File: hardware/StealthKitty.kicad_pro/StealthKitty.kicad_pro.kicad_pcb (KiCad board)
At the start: 4 copper layers, 54 x 57 mm, 89 parts, among them J1 Conn_01x08, J2 Conn_01x06, J3 Conn_01x06, J5 Conn_ST_STDC14, J7 Conn_01x06, J9 Conn_01x06, SW1 SW_Push, SW2 SW_Push, SW5 Switch, U2 ZXBM5210-S, U3 ZXBM5210-S, U4 MP1475DJ-LF-P, U5 ADXL343, U6 STM32G431CBU6, Y1 Crystal_GND24_Small

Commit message: Confirmation placement equipe
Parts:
- removed U4: MP1475DJ-LF-P, Library:SOT65P280X100-8N
- added IC501: MP1475DJ-LF-P, Library:SOT65P280X100-8N, F.Cu at (125.0, 69.0)
- moved D201 0.40 mm to (115.5, 69.6)
- moved R201 0.40 mm to (111.5, 69.6)
- moved TP309 0.25 mm to (135.0, 75.2)
- moved TP310 0.25 mm to (131.8, 75.2)
- moved C505 0.20 mm to (125.5, 64.3)
- moved R503 0.20 mm to (125.0, 65.8)
- renumbered Alim_charger2 to Alim_charger501, BT2 to BT501, C3 to C201, C4 to C202, C5 to C203, C6 to C204, C7 to C205, C8 to C206, C9 to C207, C10 to C208, C11 to C401, C19 to C402, C20 to C403, C12 to C404, C21 to C405, C1 to C406, C13 to C407, C22 to C408, C14 to C409, C23 to C410, C15 to C411, C35 to C501, C27 to C502, C26 to C503, C28 to C504, C36 to C505, C29 to C506, C39 to C507, C37 to C508, C38 to C509, Cio1 to Cio301, Cs1 to Cs301, D1 to D201, D2 to D202, D3 to D203, D4 to D204, D7 to D401, D5 to D402, D6 to D501, J2 to J201, J3 to J202, J7 to J301, J9 to J302, J1 to J303, J5 to J401, L3 to L501, PS2 to PS501, R5 to R201, R6 to R202, R7 to R203, R8 to R204, R9 to R401, R10 to R402, R17 to R403, R3 to R404, R22 to R501, R1 to R502, R23 to R503, R24 to R504, R25 to R505, R26 to R506, R21 to R507, SW1 to SW401, SW2 to SW402, SW5 to SW501, TP204 to TP203, TP203 to TP204, TP4 to TP301, TP3 to TP302, TP1 to TP303, TP2 to TP304, TP5 to TP305, TP6 to TP306, TP7 to TP307, TP9 to TP308, TP11 to TP309, TP10 to TP310, U2 to U201, U3 to U202, U5 to U301, U6 to U401, Y1 to Y401

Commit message: après première revue fiack placement
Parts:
- removed U201, U202: ZXBM5210-S, Package_SO:SOIC-8_3.9x4.9mm_P1.27mm
- added U1: ZXBM5210-SP, Package_SO:Diodes_SO-8EP, F.Cu at (113.5, 75.5)
- added U2: ZXBM5210-SP, Package_SO:Diodes_SO-8EP, F.Cu at (113.5, 91.0)
- moved Cio301 6.92 mm to (120.7, 72.1)
- moved Cs301 5.79 mm to (120.5, 75.0), turned to -90 degrees
- moved TP308 4.60 mm to (128.2, 74.6)
- moved C410 3.88 mm to (128.1, 71.6)
- moved C408 1.71 mm to (126.3, 77.2), turned to 180 degrees
- moved U301 0.32 mm to (123.1, 73.7), turned to 0 degrees
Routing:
- net +5V: track 0.00 -> 77.9 mm
- net MOSI: track 0.00 -> 9.34 mm
- net GND: vias 0 -> 17
- added copper zone on B.Cu, net GND
- added copper zone on F.Cu, net GND
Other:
- board text added: "TOF1"

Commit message: Dernier Modif 08/10/2024
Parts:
- removed D201: Blue, LED_SMD:LED_0603_1608Metric_Pad1.05x0.95mm_HandSolder
- removed D202: YELLOW, LED_SMD:LED_0603_1608Metric_Pad1.05x0.95mm_HandSolder
- removed D203: Green, LED_SMD:LED_0603_1608Metric_Pad1.05x0.95mm_HandSolder
- removed D204: RED, LED_SMD:LED_0603_1608Metric_Pad1.05x0.95mm_HandSolder
- removed R201, R202: 100R, Resistor_SMD:R_0603_1608Metric_Pad0.98x0.95mm_HandSolder
- removed R203, R204: 1k, Resistor_SMD:R_0603_1608Metric_Pad0.98x0.95mm_HandSolder
- removed TP306: TestPoint, TestPoint:TestPoint_Pad_D1.5mm
- added TP301: TestPoint, TestPoint:TestPoint_Pad_D1.5mm, F.Cu at (186.5, 93.5)
- added TP302: TestPoint, TestPoint:TestPoint_Pad_D1.5mm, F.Cu at (186.5, 97.0)
- BT501: footprint Connector_JST:JST_XH_S2B-XH-A-1_1x02_P2.50mm_Horizontal -> Connector_JST:JST_XH_S2B-XH-A_1x02_P2.50mm_Horizontal
- C201, C202, C203, C207, C208, C402, C407, C410, C504, C506, Cs301: footprint Capacitor_SMD:C_0603_1608Metric_Pad1.08x0.95mm_HandSolder -> Capacitor_SMD:C_0402_1005Metric
- C204, C205, C206, C401, C403, C404, C405, C406, C408, C409, C411, C502, C505, C508, Cio301: footprint Capacitor_SMD:C_0402_1005Metric_Pad0.74x0.62mm_HandSolder -> Capacitor_SMD:C_0402_1005Metric
- C501: value 0.1uF -> 22uF; footprint Capacitor_SMD:C_0402_1005Metric_Pad0.74x0.62mm_HandSolder -> Capacitor_SMD:C_0402_1005Metric
- C503: value 22uF -> 0.1uF; footprint Capacitor_SMD:C_0805_2012Metric_Pad1.18x1.45mm_HandSolder -> Capacitor_SMD:C_0402_1005Metric
- C507, C509: footprint Capacitor_SMD:C_0805_2012Metric_Pad1.18x1.45mm_HandSolder -> Capacitor_SMD:C_0402_1005Metric
- J301, J302: footprint Connector_JST:JST_XH_B6B-XH-A_1x06_P2.50mm_Vertical -> Connector_JST:JST_XH_S6B-XH-A_1x06_P2.50mm_Horizontal
- R401, R402, R403, R404, R501, R502, R503, R504, R505, R506, R507: footprint Resistor_SMD:R_0603_1608Metric_Pad0.98x0.95mm_HandSolder -> Resistor_SMD:R_0402_1005Metric
- SW401, SW402: footprint Button_Switch_SMD:SW_SPST_B3U-1000P -> Button_Switch_SMD:SW_Push_1P1T_NO_6x6mm_H9.5mm
- SW501: footprint Connector_JST:JST_XH_S3B-XH-A_1x03_P2.50mm_Horizontal -> Connector_JST:JST_XH_S3B-XH-A-1_1x03_P2.50mm_Horizontal
- moved TP305 76.6 mm to (187.0, 103.0)
- moved TP301 66.7 mm to (199.3, 121.0)
- moved TP302 66.7 mm to (202.3, 121.0)
- moved TP303 66.7 mm to (201.5, 118.0)
- moved TP304 66.7 mm to (204.1, 118.0)
- moved TP307 61.7 mm to (195.5, 84.3)
- moved TP309 61.7 mm to (195.5, 87.5)
- moved TP310 61.7 mm to (192.2, 87.5)
- moved J202 45.5 mm to (132.9, 99.0)
- moved C501 44.7 mm to (157.7, 90.3), turned to 0 degrees
- moved C503 42.8 mm to (157.7, 89.3), turned to 0 degrees
- moved C504 42.1 mm to (150.4, 80.8), turned to 180 degrees
- moved C509 40.5 mm to (162.3, 91.3), turned to 180 degrees
- moved PS501 40.1 mm to (150.1, 83.5), turned to -90 degrees
- moved R503 39.9 mm to (160.0, 85.0), turned to 90 degrees
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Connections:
- U401 pad 17: /brain Sheet/status_Purple -> unconnected-(U401-PB0-Pad17)
- U401 pad 18: unconnected-(U401-PB1-Pad18) -> INT2_adx
- U401 pad 19: /brain Sheet/Button_1 -> INT1_adx
- U401 pad 26: unconnected-(U401-PB13-Pad26) -> /brain Sheet/status_Orange
- U401 pad 27: /brain Sheet/status_Orange -> /brain Sheet/status_Purple
- U401 pad 28: unconnected-(U401-PB15-Pad28) -> /brain Sheet/Button_1
- U401 pad 8: INT1_adx -> unconnected-(U401-PA0-Pad8)
- U401 pad 9: INT2_adx -> unconnected-(U401-PA1-Pad9)
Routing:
- net /motorisation Sheet/Motor2-: track 0.00 -> 77.9 mm
- net +5V: track 77.9 -> 0.00 mm
- net SDA: track 0.00 -> 23.5 mm
- net SCL: track 0.00 -> 17.1 mm
- net MOSI: track 9.34 -> 0.00 mm
- net GND: vias 17 -> 25

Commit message: Modification Placement 09/10/24
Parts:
- removed the TP301 at (199.3, 121.0)
- removed the TP302 at (202.3, 121.0)
- removed TP303, TP304, TP305: TestPoint, TestPoint:TestPoint_Pad_D1.5mm
- BT501: footprint Connector_JST:JST_XH_S2B-XH-A_1x02_P2.50mm_Horizontal -> Connector_JST:JST_XH_S2B-XH-A-1_1x02_P2.50mm_Horizontal
- moved TP309 48.5 mm to (147.4, 93.4)
- moved TP310 45.0 mm to (147.4, 90.7)
- moved C404 44.8 mm to (155.8, 105.9), turned to 0 degrees
- moved C407 42.5 mm to (150.4, 95.5), turned to 0 degrees
- moved C402 41.7 mm to (154.6, 95.5), turned to 180 degrees
- moved C406 39.2 mm to (148.3, 95.5), turned to 180 degrees
- moved TP302 38.4 mm to (149.1, 88.1)
- moved C405 38.4 mm to (152.5, 95.5), turned to 0 degrees
- moved TP307 37.8 mm to (159.3, 95.2)
- moved C401 35.3 mm to (147.3, 102.5), turned to 90 degrees
- moved TP301 27.6 mm to (159.3, 98.2)
- moved R401 4.07 mm to (155.8, 117.2)
- moved C408 2.80 mm to (156.5, 92.2)
- moved R402 2.28 mm to (158.1, 117.2)
- moved C410 2.20 mm to (149.5, 92.3)
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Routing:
- net SDA: track 23.5 -> 0.00 mm
- net SCL: track 17.1 -> 0.00 mm
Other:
- board size 54 x 57 mm -> 54 x 58.9 mm

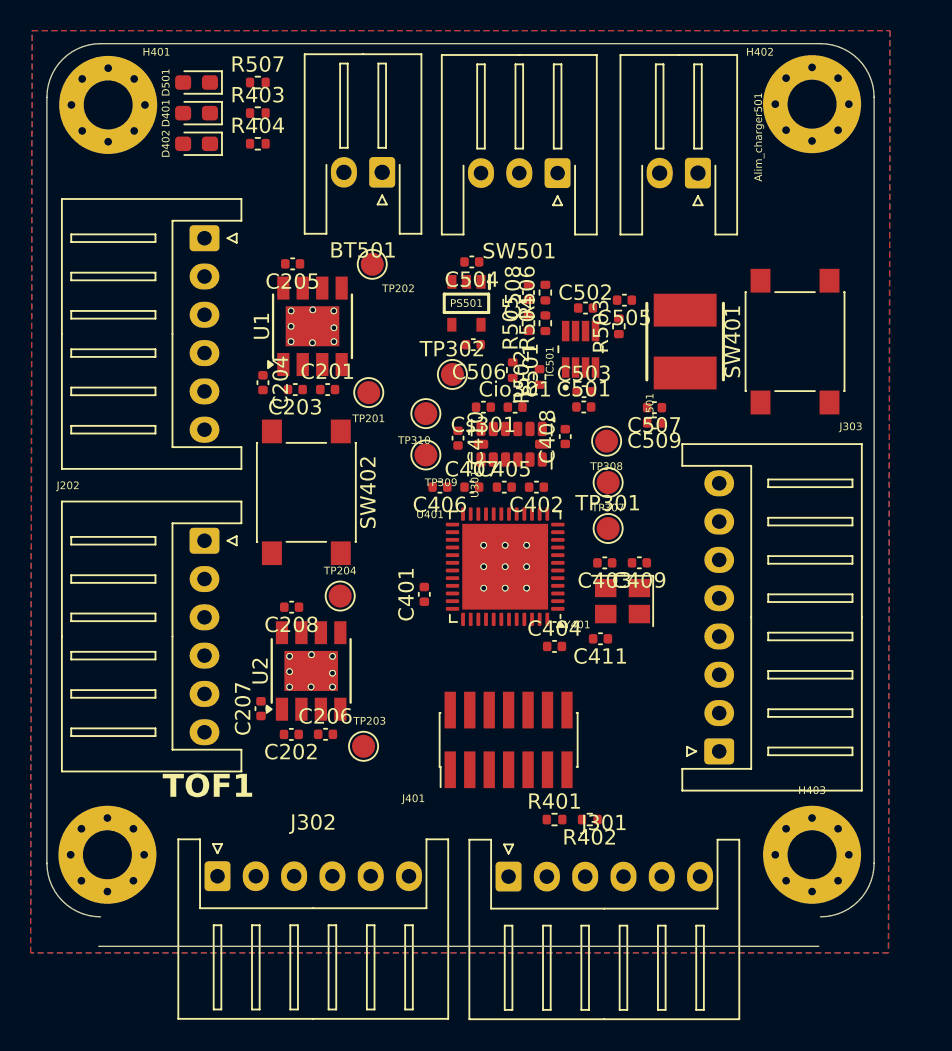
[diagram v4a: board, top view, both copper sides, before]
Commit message: Début routage
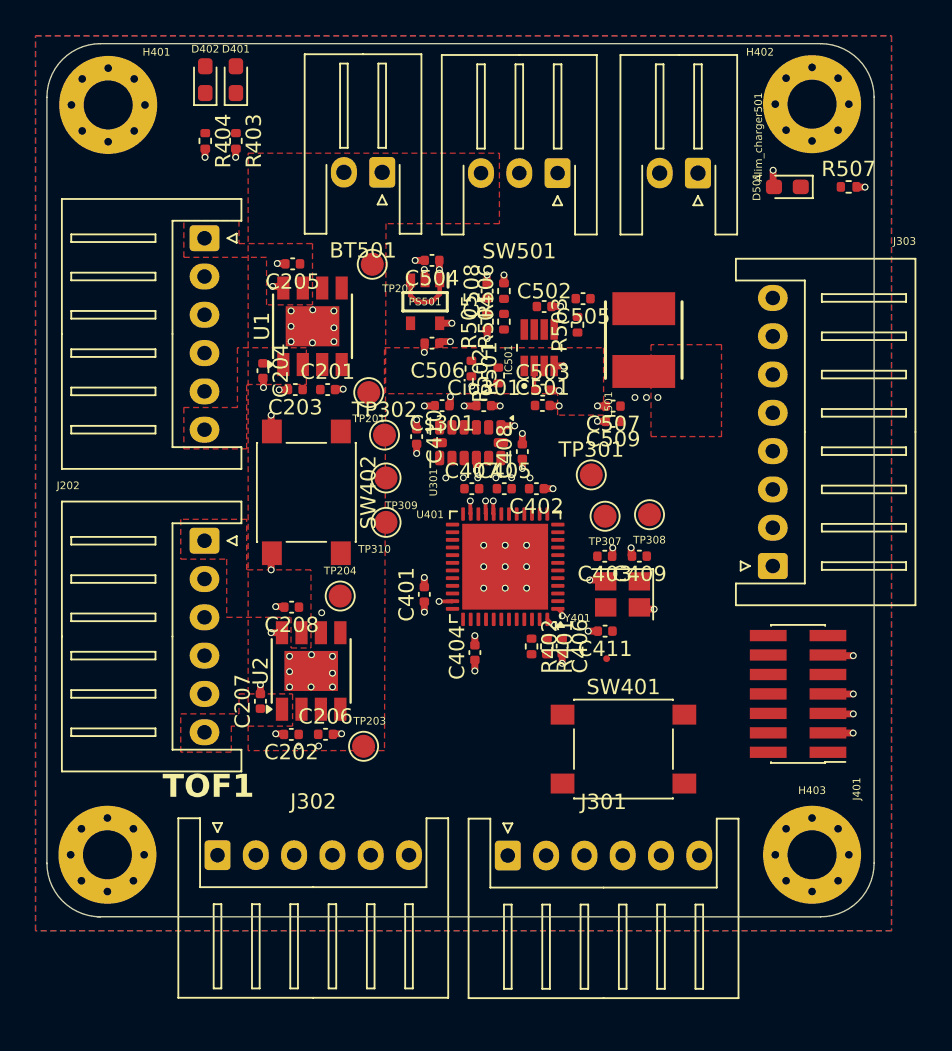
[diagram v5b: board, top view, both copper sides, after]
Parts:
- moved D501 39.2 mm to (171.0, 75.9)
- moved R507 39.2 mm to (175.0, 75.9)
- moved SW401 28.9 mm to (160.3, 112.6), turned to 0 degrees
- moved J401 19.1 mm to (171.7, 109.0), turned to 180 degrees
- moved C406 13.1 mm to (156.3, 105.9), turned to -90 degrees
- moved J303 12.6 mm to (170.1, 100.7)
- moved R402 11.9 mm to (154.3, 105.9), turned to -90 degrees
- moved R401 11.3 mm to (155.3, 105.9), turned to -90 degrees
- moved TP310 7.56 mm to (144.8, 97.8)
- moved TP302 5.94 mm to (144.7, 92.1)
- moved TP308 5.56 mm to (162.0, 97.3)
- moved C404 5.22 mm to (150.6, 106.3), turned to 90 degrees
- moved D402 4.22 mm to (133.0, 68.9), turned to 90 degrees
- moved TP301 3.67 mm to (158.2, 94.7)
- moved R404 3.44 mm to (133.0, 72.9), turned to -90 degrees
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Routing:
- net /motorisation Sheet/Motor2-: track 77.9 -> 0.00 mm
- net +5V: track 0.00 -> 70.9 mm, vias 0 -> 6
- net GND: track 0.00 -> 30.7 mm, vias 25 -> 70
- net +3.3V: track 0.00 -> 14.2 mm, vias 0 -> 21
- net +VBAT: track 0.00 -> 1.61 mm, vias 0 -> 4
- added copper zone on F.Cu, net +5V
- added copper zone on In2.Cu, net +5V
- added copper zone on F.Cu, net +VBAT
- added copper zone on In2.Cu, net +VBAT
- added copper zone on F.Cu, net /motorisation Sheet/Motor1+
- added copper zone on F.Cu, net /motorisation Sheet/Motor1-
- added copper zone on F.Cu, net /motorisation Sheet/Motor2+
- added copper zone on F.Cu, net /motorisation Sheet/Motor2-
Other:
- board size 54 x 58.9 mm -> 54 x 57 mm

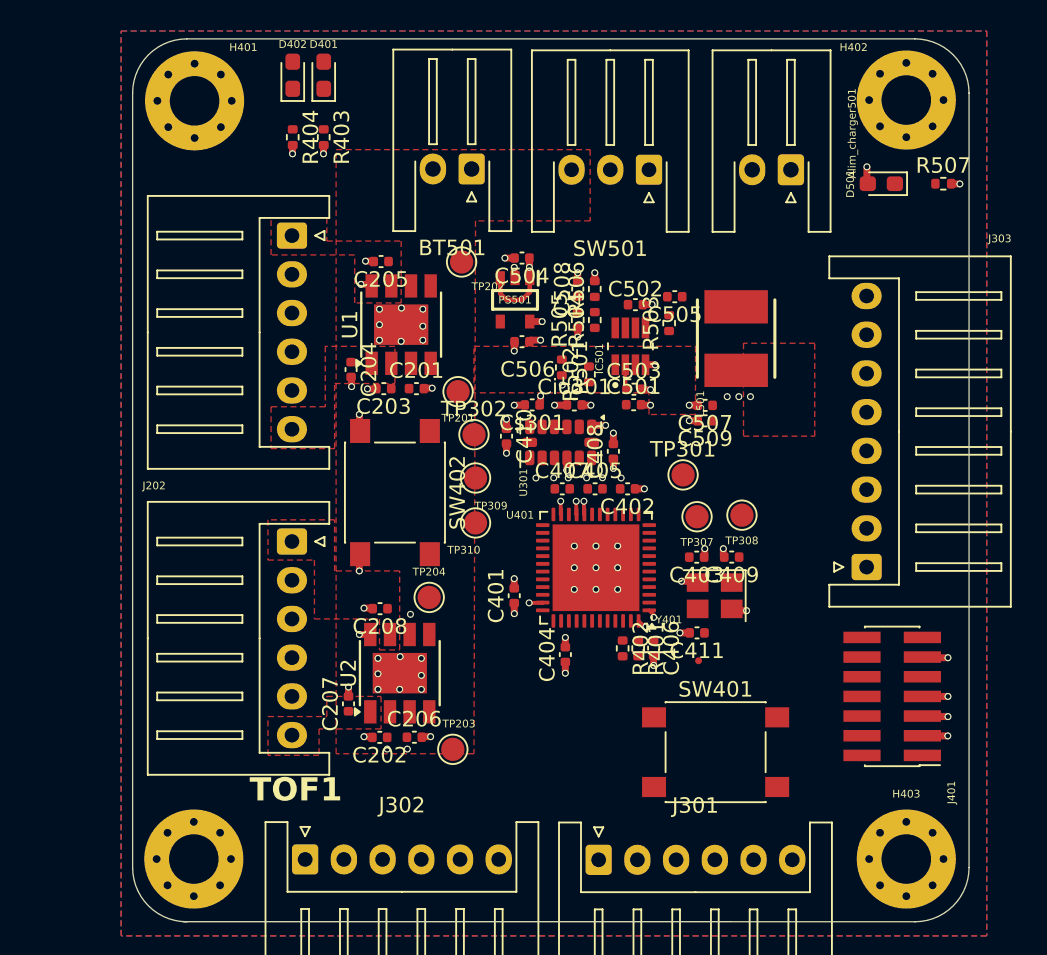
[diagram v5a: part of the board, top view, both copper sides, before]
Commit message: MAJ première version routage
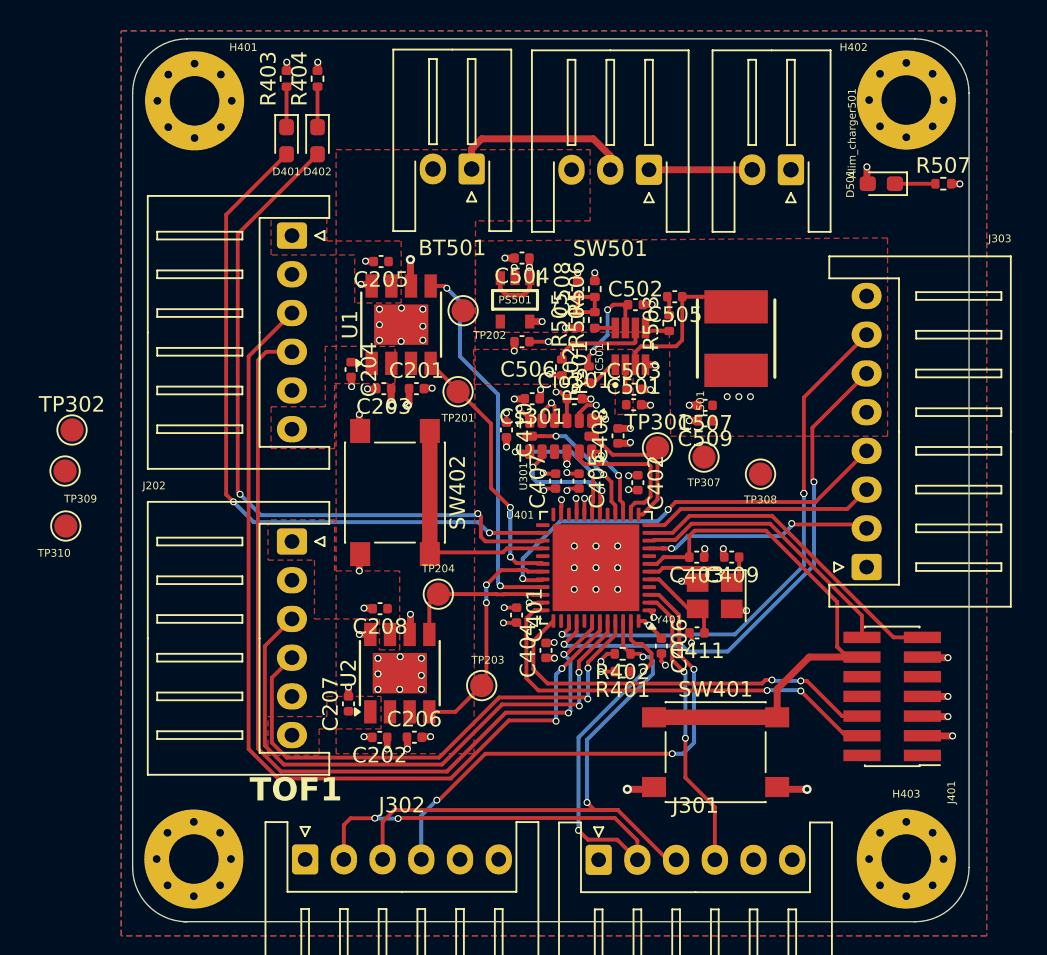
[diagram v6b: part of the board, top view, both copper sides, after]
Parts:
- moved TP309 26.5 mm to (118.3, 94.5)
- moved TP310 26.5 mm to (118.3, 98.0)
- moved TP302 26.0 mm to (118.8, 91.8)
- moved D401 4.86 mm to (132.6, 73.1), turned to -90 degrees
- moved TP203 4.52 mm to (145.2, 108.3)
- moved D402 4.52 mm to (134.6, 73.1), turned to -90 degrees
- moved R403 4.47 mm to (132.6, 69.1), turned to 90 degrees
- moved R404 4.10 mm to (134.6, 69.1), turned to 90 degrees
- moved TP307 3.88 mm to (159.6, 93.5)
- moved TP202 3.15 mm to (144.0, 84.1)
- moved TP308 2.91 mm to (163.2, 94.7)
- moved TP301 2.41 mm to (156.6, 93.0)
- moved R401 1.80 mm to (154.3, 107.4), turned to 180 degrees
- moved C404 1.28 mm to (149.3, 106.0)
- moved C401 1.26 mm to (147.4, 103.8), turned to -90 degrees
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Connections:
- U401 pad 12: unconnected-(U401-PA4-Pad12) -> DEV_EN
- U401 pad 22: M_EN -> unconnected-(U401-PB10-Pad22)
- U401 pad 24: DEV_EN -> unconnected-(U401-PB11-Pad24)
- U401 pad 9: unconnected-(U401-PA1-Pad9) -> M_EN
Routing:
- net Codeur1_PH2: track 0.00 -> 59.3 mm, vias 0 -> 2
- net Codeur1_PH1: track 0.00 -> 56.8 mm, vias 0 -> 2
- net /brain Sheet/status_Purple: track 0.00 -> 45.8 mm, vias 0 -> 2
- net /brain Sheet/status_Orange: track 0.00 -> 45.0 mm, vias 0 -> 2
- net SDA: track 0.00 -> 44.3 mm, vias 0 -> 4
- net SCL: track 0.00 -> 40.1 mm, vias 0 -> 2
- net Codeur2_PH1: track 0.00 -> 37.6 mm, vias 0 -> 2
- net /brain Sheet/NRST: track 0.00 -> 36.7 mm
- net Tx_Lidar: track 0.00 -> 35.2 mm, vias 0 -> 3
- net Rx_lidar: track 0.00 -> 34.3 mm, vias 0 -> 2
- net Codeur2_PH2: track 0.00 -> 34.2 mm, vias 0 -> 2
- net INT_tof2: track 0.00 -> 33.5 mm, vias 0 -> 3
- net /brain Sheet/SWDIO: track 0.00 -> 28.4 mm, vias 0 -> 2
- net M_SCTR: track 0.00 -> 27.8 mm, vias 0 -> 2
- net /brain Sheet/SWCLK: track 0.00 -> 26.4 mm, vias 0 -> 2
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
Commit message: Modif Routage V2
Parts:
- moved TP309 29.1 mm to (147.4, 95.3)
- moved TP310 27.4 mm to (145.3, 93.2)
- moved TP301 3.56 mm to (159.8, 94.4)
- moved TP307 2.50 mm to (157.2, 94.4)
- moved TP308 0.61 mm to (162.7, 94.3)
- moved C410 0.30 mm to (146.8, 91.5)
- moved TP202 0.10 mm to (143.9, 84.1)
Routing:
- net SCK: track 8.94 -> 15.9 mm
- net INT2_adx: track 8.35 -> 11.2 mm
- net INT1_adx: track 9.21 -> 11.2 mm
- net MISO: track 9.27 -> 11.0 mm
- net PWM_MOT1_CH1: track 16.9 -> 18.2 mm
- net PWM_MOT2_CH2: track 9.62 -> 8.42 mm
- net PWM_MOT1_CH2: track 24.5 -> 25.7 mm

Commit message: Modif Routage V3
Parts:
- Driver 1: renamed from U1
- Driver 2: renamed from U2
- NRST SW: renamed from SW401
- PWM1 CH1: renamed from TP201
- PWM1 CH2: renamed from TP202
- PWM2 CH1: renamed from TP203
- PWM2 CH2: renamed from TP204
- moved nCS 28.1 mm to (146.6, 88.2)
- renumbered Alim_charger501 to Alim_charger, SW402 to Button_1, TP310 to INT1, TP309 to INT2, J303 to LIDAR, TP307 to MISO, TP308 to MOSI, Y401 to Quartz, TP301 to SCK, J401 to STLink, D401 to Status_Orange, D402 to Status_Purple, J301 to TOF2, TP302 to nCS
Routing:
- net nCS: track 8.70 -> 20.7 mm, vias 2 -> 3
- net MOSI: track 5.27 -> 15.5 mm
- net SCL: track 40.1 -> 42.4 mm
- net +3.3V: track 23.7 -> 24.3 mm
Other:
- board text added: "MOTOR 1"
- board text added: "MOTOR 2"
- board text added: "TOF2"
